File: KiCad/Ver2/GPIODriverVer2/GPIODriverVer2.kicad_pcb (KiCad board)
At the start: 4 copper layers, 50 x 50 mm, 52 parts, among them J2 ExtInputs, J3 DaisyChainInput, J4 DaisyChainOutput, J5 DriveOutput, Q1 2N3904, Q2 AOD409, Q3 2N3904, Q4 MMBT5401, Q5 MMBT5551L, U1 SR_WRITE_HI, U10 74LVC1G3157, U11 74LVC1G3157, U12 74LVC1G3157, U13 74LVC1G3157, U14 74LVC1G3157, U15 74HC244, U16 74HC244, U17 74HC244, U2 SR_WRITE_LO, U3 SR_READ_STATE, U4 74LVC1G3157, U5 LTV-357T, U6 74LVC1G3157, U7 74LVC1G3157, U8 74LVC1G3157, U9 74LVC1G3157

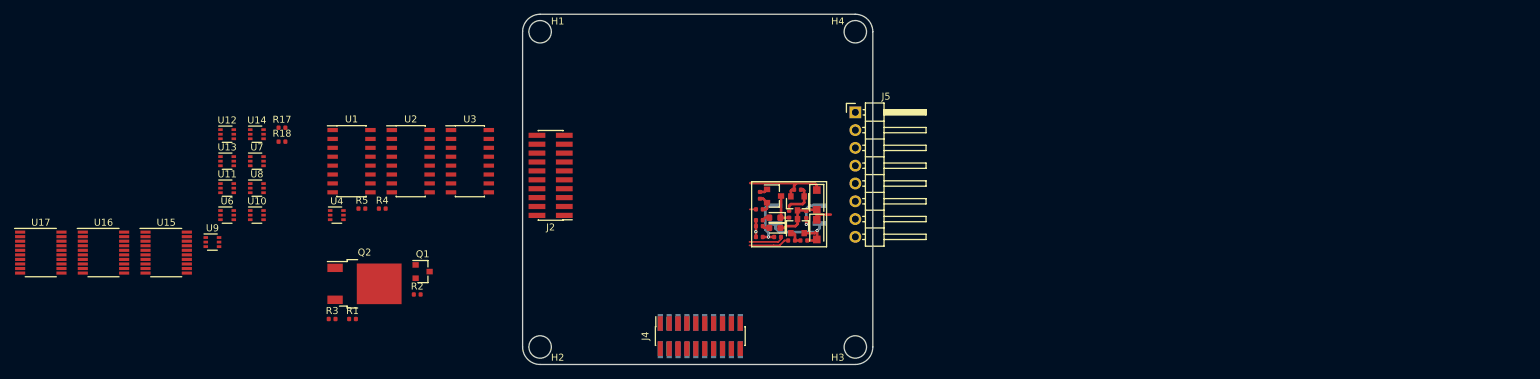
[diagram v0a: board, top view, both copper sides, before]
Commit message: Add sheets for output drive channels.
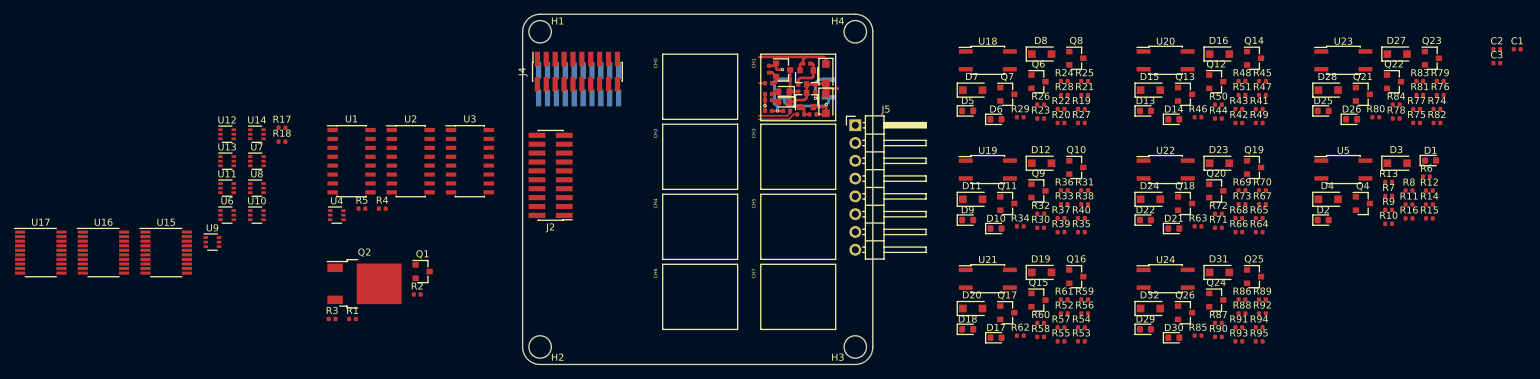
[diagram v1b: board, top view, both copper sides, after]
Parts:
- added C1: 100nF, Capacitor_SMD:C_0402_1005Metric, F.Cu at (242.0, 105.0)
- added C2: 100nF, Capacitor_SMD:C_0402_1005Metric, F.Cu at (239.1, 105.0)
- added C3: 100nF, Capacitor_SMD:C_0402_1005Metric, F.Cu at (239.1, 107.0)
- added D1: LED_HI_DRIVE_EN, Diode_SMD:D_0603_1608Metric, F.Cu at (229.6, 120.9)
- added D10: LED_LO_DRIVE_EN, Diode_SMD:D_0603_1608Metric, F.Cu at (167.6, 130.6)
- added D11: 1N4007, Diode_SMD:D_SOD-123F, F.Cu at (164.3, 126.4)
- added D12: 1N4007, Diode_SMD:D_SOD-123F, F.Cu at (174.1, 121.3)
- added D13: LED_HI_DRIVE_EN, Diode_SMD:D_0603_1608Metric, F.Cu at (188.9, 113.8)
- added D14: LED_LO_DRIVE_EN, Diode_SMD:D_0603_1608Metric, F.Cu at (193.0, 115.0)
- added D15: 1N4007, Diode_SMD:D_SOD-123F, F.Cu at (189.6, 110.8)
- added D16: 1N4007, Diode_SMD:D_SOD-123F, F.Cu at (199.5, 105.7)
- added D17: LED_HI_DRIVE_EN, Diode_SMD:D_0603_1608Metric, F.Cu at (167.6, 146.2)
- added D18: LED_LO_DRIVE_EN, Diode_SMD:D_0603_1608Metric, F.Cu at (163.5, 145.0)
- added D19: 1N4007, Diode_SMD:D_SOD-123F, F.Cu at (174.1, 136.9)
- added D2: LED_LO_DRIVE_EN, Diode_SMD:D_0603_1608Metric, F.Cu at (214.3, 129.4)
- added D20: 1N4007, Diode_SMD:D_SOD-123F, F.Cu at (164.3, 142.0)
- added D21: LED_HI_DRIVE_EN, Diode_SMD:D_0603_1608Metric, F.Cu at (193.0, 130.6)
- added D22: LED_LO_DRIVE_EN, Diode_SMD:D_0603_1608Metric, F.Cu at (188.9, 129.4)
- added D23: 1N4007, Diode_SMD:D_SOD-123F, F.Cu at (199.5, 121.3)
- added D24: 1N4007, Diode_SMD:D_SOD-123F, F.Cu at (189.6, 126.4)
- added D25: LED_HI_DRIVE_EN, Diode_SMD:D_0603_1608Metric, F.Cu at (214.3, 113.8)
- added D26: LED_LO_DRIVE_EN, Diode_SMD:D_0603_1608Metric, F.Cu at (218.3, 115.0)
- added D27: 1N4007, Diode_SMD:D_SOD-123F, F.Cu at (224.9, 105.7)
- added D28: 1N4007, Diode_SMD:D_SOD-123F, F.Cu at (215.0, 110.8)
- added D29: LED_HI_DRIVE_EN, Diode_SMD:D_0603_1608Metric, F.Cu at (188.9, 145.0)
- added D3: 1N4007, Diode_SMD:D_SOD-123F, F.Cu at (224.9, 121.3)
- added D30: LED_LO_DRIVE_EN, Diode_SMD:D_0603_1608Metric, F.Cu at (193.0, 146.2)
- added D31: 1N4007, Diode_SMD:D_SOD-123F, F.Cu at (199.5, 136.9)
- added D32: 1N4007, Diode_SMD:D_SOD-123F, F.Cu at (189.6, 142.0)
- added D4: 1N4007, Diode_SMD:D_SOD-123F, F.Cu at (215.0, 126.4)
- added D5: LED_HI_DRIVE_EN, Diode_SMD:D_0603_1608Metric, F.Cu at (163.5, 113.8)
- added D6: LED_LO_DRIVE_EN, Diode_SMD:D_0603_1608Metric, F.Cu at (167.6, 115.0)
- added D7: 1N4007, Diode_SMD:D_SOD-123F, F.Cu at (164.3, 110.8)
- added D8: 1N4007, Diode_SMD:D_SOD-123F, F.Cu at (174.1, 105.7)
- added D9: LED_HI_DRIVE_EN, Diode_SMD:D_0603_1608Metric, F.Cu at (163.5, 129.4)
- added Q10: MMBT5401, Package_TO_SOT_SMD:SOT-23, F.Cu at (179.1, 121.9)
- added Q11: MMBT5551L, Package_TO_SOT_SMD:SOT-23, F.Cu at (169.2, 127.0)
- added Q12: 2N3904, Package_TO_SOT_SMD:SOT-23, F.Cu at (199.0, 109.6)
- added Q13: MMBT5401, Package_TO_SOT_SMD:SOT-23, F.Cu at (194.6, 111.4)
- added Q14: MMBT5551L, Package_TO_SOT_SMD:SOT-23, F.Cu at (204.4, 106.3)
- added Q15: 2N3904, Package_TO_SOT_SMD:SOT-23, F.Cu at (173.7, 140.8)
- added Q16: MMBT5401, Package_TO_SOT_SMD:SOT-23, F.Cu at (179.1, 137.5)
- added Q17: MMBT5551L, Package_TO_SOT_SMD:SOT-23, F.Cu at (169.2, 142.6)
- added Q18: 2N3904, Package_TO_SOT_SMD:SOT-23, F.Cu at (194.6, 127.0)
- added Q19: MMBT5401, Package_TO_SOT_SMD:SOT-23, F.Cu at (204.4, 121.9)
- added Q20: MMBT5551L, Package_TO_SOT_SMD:SOT-23, F.Cu at (199.0, 125.2)
- added Q21: 2N3904, Package_TO_SOT_SMD:SOT-23, F.Cu at (220.0, 111.4)
- added Q22: MMBT5401, Package_TO_SOT_SMD:SOT-23, F.Cu at (224.4, 109.6)
- added Q23: MMBT5551L, Package_TO_SOT_SMD:SOT-23, F.Cu at (229.8, 106.3)
- added Q24: 2N3904, Package_TO_SOT_SMD:SOT-23, F.Cu at (199.0, 140.8)
- added Q25: MMBT5401, Package_TO_SOT_SMD:SOT-23, F.Cu at (204.4, 137.5)
- added Q26: MMBT5551L, Package_TO_SOT_SMD:SOT-23, F.Cu at (194.6, 142.6)
- added Q4: MMBT5401, Package_TO_SOT_SMD:SOT-23, F.Cu at (220.0, 127.0)
- added Q6: 2N3904, Package_TO_SOT_SMD:SOT-23, F.Cu at (173.7, 109.6)
- added Q7: MMBT5401, Package_TO_SOT_SMD:SOT-23, F.Cu at (169.2, 111.4)
- added Q8: MMBT5551L, Package_TO_SOT_SMD:SOT-23, F.Cu at (179.1, 106.3)
- added Q9: 2N3904, Package_TO_SOT_SMD:SOT-23, F.Cu at (173.7, 125.2)
- added R10: 10k, Resistor_SMD:R_0402_1005Metric, F.Cu at (223.6, 129.9)
- added R11: 500, Resistor_SMD:R_0402_1005Metric, F.Cu at (226.6, 127.2)
- added R12: 1.8k, Resistor_SMD:R_0402_1005Metric, F.Cu at (229.5, 125.2)
- added R13: 100, Resistor_SMD:R_0402_1005Metric, F.Cu at (223.6, 123.9)
- added R14: 10k, Resistor_SMD:R_0402_1005Metric, F.Cu at (229.5, 127.2)
- added R15: 10k, Resistor_SMD:R_0402_1005Metric, F.Cu at (229.5, 129.2)
- added R16: 5.6k, Resistor_SMD:R_0402_1005Metric, F.Cu at (226.6, 129.2)
- added R19: 1.8k, Resistor_SMD:R_0402_1005Metric, F.Cu at (179.8, 113.5)
- added R20: 100, Resistor_SMD:R_0402_1005Metric, F.Cu at (176.9, 115.5)
- added R21: 10k, Resistor_SMD:R_0402_1005Metric, F.Cu at (180.2, 111.5)
- added R22: 100, Resistor_SMD:R_0402_1005Metric, F.Cu at (176.9, 113.5)
- added R23: 10k, Resistor_SMD:R_0402_1005Metric, F.Cu at (174.0, 114.9)
- added R24: 500, Resistor_SMD:R_0402_1005Metric, F.Cu at (177.3, 109.5)
- added R25: 1.8k, Resistor_SMD:R_0402_1005Metric, F.Cu at (180.2, 109.5)
- added R26: 100, Resistor_SMD:R_0402_1005Metric, F.Cu at (174.0, 112.9)
- added R27: 10k, Resistor_SMD:R_0402_1005Metric, F.Cu at (179.8, 115.5)
- added R28: 10k, Resistor_SMD:R_0402_1005Metric, F.Cu at (177.3, 111.5)
- added R29: 5.6k, Resistor_SMD:R_0402_1005Metric, F.Cu at (171.1, 114.7)
- added R30: 1.8k, Resistor_SMD:R_0402_1005Metric, F.Cu at (174.0, 130.5)
- added R31: 100, Resistor_SMD:R_0402_1005Metric, F.Cu at (180.2, 125.1)
- added R32: 10k, Resistor_SMD:R_0402_1005Metric, F.Cu at (174.0, 128.5)
- added R33: 100, Resistor_SMD:R_0402_1005Metric, F.Cu at (177.3, 127.1)
- added R34: 10k, Resistor_SMD:R_0402_1005Metric, F.Cu at (171.1, 130.3)
- added R35: 500, Resistor_SMD:R_0402_1005Metric, F.Cu at (179.8, 131.1)
- added R36: 1.8k, Resistor_SMD:R_0402_1005Metric, F.Cu at (177.3, 125.1)
- added R37: 100, Resistor_SMD:R_0402_1005Metric, F.Cu at (176.9, 129.1)
- added R38: 10k, Resistor_SMD:R_0402_1005Metric, F.Cu at (180.2, 127.1)
- added R39: 10k, Resistor_SMD:R_0402_1005Metric, F.Cu at (176.9, 131.1)
- added R40: 5.6k, Resistor_SMD:R_0402_1005Metric, F.Cu at (179.8, 129.1)
- added R41: 1.8k, Resistor_SMD:R_0402_1005Metric, F.Cu at (205.2, 113.5)
- added R42: 100, Resistor_SMD:R_0402_1005Metric, F.Cu at (202.2, 115.5)
- added R43: 10k, Resistor_SMD:R_0402_1005Metric, F.Cu at (202.2, 113.5)
- added R44: 100, Resistor_SMD:R_0402_1005Metric, F.Cu at (199.3, 114.9)
- added R45: 10k, Resistor_SMD:R_0402_1005Metric, F.Cu at (205.6, 109.5)
- added R46: 500, Resistor_SMD:R_0402_1005Metric, F.Cu at (196.4, 114.7)
- added R47: 1.8k, Resistor_SMD:R_0402_1005Metric, F.Cu at (205.6, 111.5)
- added R48: 100, Resistor_SMD:R_0402_1005Metric, F.Cu at (202.7, 109.5)
- added R49: 10k, Resistor_SMD:R_0402_1005Metric, F.Cu at (205.2, 115.5)
- added R50: 10k, Resistor_SMD:R_0402_1005Metric, F.Cu at (199.3, 112.9)
- added R51: 5.6k, Resistor_SMD:R_0402_1005Metric, F.Cu at (202.7, 111.5)
- added R52: 1.8k, Resistor_SMD:R_0402_1005Metric, F.Cu at (177.3, 142.7)
- added R53: 100, Resistor_SMD:R_0402_1005Metric, F.Cu at (179.8, 146.7)
- added R54: 10k, Resistor_SMD:R_0402_1005Metric, F.Cu at (179.8, 144.7)
- added R55: 100, Resistor_SMD:R_0402_1005Metric, F.Cu at (176.9, 146.7)
- added R56: 10k, Resistor_SMD:R_0402_1005Metric, F.Cu at (180.2, 142.7)
- added R57: 500, Resistor_SMD:R_0402_1005Metric, F.Cu at (176.9, 144.7)
- added R58: 1.8k, Resistor_SMD:R_0402_1005Metric, F.Cu at (174.0, 146.1)
- added R59: 100, Resistor_SMD:R_0402_1005Metric, F.Cu at (180.2, 140.7)
- added R6: 1.8k, Resistor_SMD:R_0402_1005Metric, F.Cu at (229.0, 123.2)
- added R60: 10k, Resistor_SMD:R_0402_1005Metric, F.Cu at (174.0, 144.1)
- added R61: 10k, Resistor_SMD:R_0402_1005Metric, F.Cu at (177.3, 140.7)
- added R62: 5.6k, Resistor_SMD:R_0402_1005Metric, F.Cu at (171.1, 145.9)
- added R63: 1.8k, Resistor_SMD:R_0402_1005Metric, F.Cu at (196.4, 130.3)
- added R64: 100, Resistor_SMD:R_0402_1005Metric, F.Cu at (205.2, 131.1)
- added R65: 10k, Resistor_SMD:R_0402_1005Metric, F.Cu at (205.2, 129.1)
- added R66: 100, Resistor_SMD:R_0402_1005Metric, F.Cu at (202.2, 131.1)
- added R67: 10k, Resistor_SMD:R_0402_1005Metric, F.Cu at (205.6, 127.1)
- added R68: 500, Resistor_SMD:R_0402_1005Metric, F.Cu at (202.2, 129.1)
- added R69: 1.8k, Resistor_SMD:R_0402_1005Metric, F.Cu at (202.7, 125.1)
- added R7: 100, Resistor_SMD:R_0402_1005Metric, F.Cu at (223.6, 125.9)
- added R70: 100, Resistor_SMD:R_0402_1005Metric, F.Cu at (205.6, 125.1)
- added R71: 10k, Resistor_SMD:R_0402_1005Metric, F.Cu at (199.3, 130.5)
- added R72: 10k, Resistor_SMD:R_0402_1005Metric, F.Cu at (199.3, 128.5)
- added R73: 5.6k, Resistor_SMD:R_0402_1005Metric, F.Cu at (202.7, 127.1)
- added R74: 1.8k, Resistor_SMD:R_0402_1005Metric, F.Cu at (230.5, 113.5)
- added R75: 100, Resistor_SMD:R_0402_1005Metric, F.Cu at (227.6, 115.5)
- added R76: 10k, Resistor_SMD:R_0402_1005Metric, F.Cu at (231.0, 111.5)
- added R77: 100, Resistor_SMD:R_0402_1005Metric, F.Cu at (227.6, 113.5)
- added R78: 10k, Resistor_SMD:R_0402_1005Metric, F.Cu at (224.7, 114.9)
- added R79: 500, Resistor_SMD:R_0402_1005Metric, F.Cu at (231.0, 109.5)
- added R8: 10k, Resistor_SMD:R_0402_1005Metric, F.Cu at (226.6, 125.2)
- added R80: 1.8k, Resistor_SMD:R_0402_1005Metric, F.Cu at (221.8, 114.7)
- added R81: 100, Resistor_SMD:R_0402_1005Metric, F.Cu at (228.1, 111.5)
- added R82: 10k, Resistor_SMD:R_0402_1005Metric, F.Cu at (230.5, 115.5)
- added R83: 10k, Resistor_SMD:R_0402_1005Metric, F.Cu at (228.1, 109.5)
- added R84: 5.6k, Resistor_SMD:R_0402_1005Metric, F.Cu at (224.7, 112.9)
- added R85: 1.8k, Resistor_SMD:R_0402_1005Metric, F.Cu at (196.4, 145.9)
- added R86: 100, Resistor_SMD:R_0402_1005Metric, F.Cu at (202.7, 140.7)
- added R87: 10k, Resistor_SMD:R_0402_1005Metric, F.Cu at (199.3, 144.1)
- added R88: 100, Resistor_SMD:R_0402_1005Metric, F.Cu at (202.7, 142.7)
- added R89: 10k, Resistor_SMD:R_0402_1005Metric, F.Cu at (205.6, 140.7)
- added R9: 100, Resistor_SMD:R_0402_1005Metric, F.Cu at (223.6, 127.9)
- added R90: 500, Resistor_SMD:R_0402_1005Metric, F.Cu at (199.3, 146.1)
- added R91: 1.8k, Resistor_SMD:R_0402_1005Metric, F.Cu at (202.2, 144.7)
- added R92: 100, Resistor_SMD:R_0402_1005Metric, F.Cu at (205.6, 142.7)
- added R93: 10k, Resistor_SMD:R_0402_1005Metric, F.Cu at (202.2, 146.7)
- added R94: 10k, Resistor_SMD:R_0402_1005Metric, F.Cu at (205.2, 144.7)
- added R95: 5.6k, Resistor_SMD:R_0402_1005Metric, F.Cu at (205.2, 146.7)
- added U18: LTV-357T, Package_SO:SO-4_4.4x3.6mm_P2.54mm, F.Cu at (166.4, 106.6)
- added U19: LTV-357T, Package_SO:SO-4_4.4x3.6mm_P2.54mm, F.Cu at (166.4, 122.2)
- added U20: LTV-357T, Package_SO:SO-4_4.4x3.6mm_P2.54mm, F.Cu at (191.8, 106.6)
- added U21: LTV-357T, Package_SO:SO-4_4.4x3.6mm_P2.54mm, F.Cu at (166.4, 137.8)
- added U22: LTV-357T, Package_SO:SO-4_4.4x3.6mm_P2.54mm, F.Cu at (191.8, 122.2)
- added U23: LTV-357T, Package_SO:SO-4_4.4x3.6mm_P2.54mm, F.Cu at (217.2, 106.6)
- added U24: LTV-357T, Package_SO:SO-4_4.4x3.6mm_P2.54mm, F.Cu at (191.8, 137.8)
- added U5: LTV-357T, Package_SO:SO-4_4.4x3.6mm_P2.54mm, F.Cu at (217.2, 122.2)
- moved J4 41.6 mm to (107.8, 108.2)
- moved J3 39.9 mm to (108.0, 110.0)
- moved D1 18.0 mm to (137.3, 111.0)
- moved R10 18.0 mm to (135.1, 113.8)
- moved R11 18.0 mm to (139.3, 110.5)
- moved R13 18.0 mm to (139.7, 114.3)
- moved R15 18.0 mm to (141.4, 114.3)
- moved R9 18.0 mm to (137.7, 113.8)
- moved D2 18.0 mm to (137.3, 112.5)
- moved D3 18.0 mm to (143.3, 108.5)
- moved D4 18.0 mm to (143.3, 112.8)
- moved Q4 18.0 mm to (140.6, 109.0)
- moved Q5 18.0 mm to (140.6, 112.2)
- moved R14 18.0 mm to (140.6, 107.0)
- moved R16 18.0 mm to (141.8, 110.6)
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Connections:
- J5 pad 1: Net-(J5-Pad1) -> /DriveCircuitry/DriveChannel0/DriveOutput
- J5 pad 3: Net-(J5-Pad3) -> /DriveCircuitry/DriveChannel2/DriveOutput
- J5 pad 4: Net-(J5-Pad4) -> /DriveCircuitry/DriveChannel3/DriveOutput
- J5 pad 5: Net-(J5-Pad5) -> /DriveCircuitry/DriveChannel4/DriveOutput
- J5 pad 6: Net-(J5-Pad6) -> /DriveCircuitry/DriveChannel5/DriveOutput
- J5 pad 7: Net-(J5-Pad7) -> /DriveCircuitry/DriveChannel6/DriveOutput
- J5 pad 8: Net-(J5-Pad8) -> /DriveCircuitry/DriveChannel7/DriveOutput
- U1 pad 15: Net-(U1-Pad15) -> CH0_HI_EN
- U1 pad 2: Net-(U1-Pad2) -> CH2_HI_EN
- U1 pad 3: Net-(U1-Pad3) -> CH3_HI_EN
- U1 pad 4: Net-(U1-Pad4) -> CH4_HI_EN
- U1 pad 5: Net-(U1-Pad5) -> CH5_HI_EN
- U1 pad 6: Net-(U1-Pad6) -> CH6_HI_EN
- U1 pad 7: Net-(U1-Pad7) -> CH7_HI_EN
- U2 pad 15: Net-(U2-Pad15) -> CH0_LO_EN
- U2 pad 2: Net-(U2-Pad2) -> CH2_LO_EN
- U2 pad 3: Net-(U2-Pad3) -> CH3_LO_EN
- U2 pad 4: Net-(U2-Pad4) -> CH4_LO_EN
- U2 pad 5: Net-(U2-Pad5) -> CH5_LO_EN
- U2 pad 6: Net-(U2-Pad6) -> CH6_LO_EN
- U2 pad 7: Net-(U2-Pad7) -> CH7_LO_EN
- U3 pad 11: Net-(U3-Pad11) -> CH0_STATE
- U3 pad 13: Net-(U3-Pad13) -> CH2_STATE
- U3 pad 14: Net-(U3-Pad14) -> CH3_STATE
- U3 pad 3: Net-(U3-Pad3) -> CH4_STATE
- U3 pad 4: Net-(U3-Pad4) -> CH5_STATE
- U3 pad 5: Net-(U3-Pad5) -> CH6_STATE
- U3 pad 6: Net-(U3-Pad6) -> CH7_STATE
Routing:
- net GND: track 14.0 -> 15.7 mm, vias 1 -> 2
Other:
- board text added: "CH0"
- board text added: "CH1"
- board text added: "CH2"
- board text added: "CH3"
- board text added: "CH4"
- board text added: "CH5"
- board text added: "CH6"
- board text added: "CH7"
